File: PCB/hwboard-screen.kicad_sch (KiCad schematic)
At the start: 1 part, among them J1 Conn_01x40

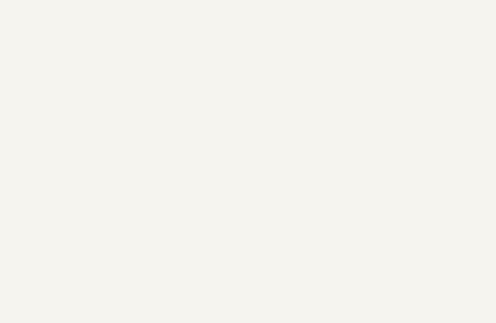
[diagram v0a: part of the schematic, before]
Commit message: add resistive touch IC
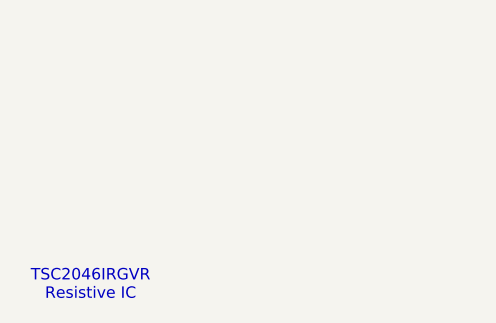
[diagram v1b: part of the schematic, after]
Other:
- note added: "TSC2046IRGVR Resistive IC"
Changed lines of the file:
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@@
 	(generator_version "9.0")
 	(paper "A4")
+	(text "TSC2046IRGVR\nResistive IC"
+		(exclude_from_sim no)
+		(at 111.252 159.258 0)
+		(effects
+			(font
+				(size 1.27 1.27)
+			)
+		)
+	)
 	(symbol
 		(lib_id "Connector_Generic:Conn_01x40")

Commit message: add maybe layout and pcb for screen
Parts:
- removed J1: Conn_01x40, symbol Connector_Generic:Conn_01x40
- added DISP1: QD3508, G__project_3.5inch_3.5inch_common_spi_ctp_PCB_3.5inch_Common_SPI_CTP.PcbLib:3.5-QD3503, symbol hwboard-bike-computer:QD3508
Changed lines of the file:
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@@
 	)
 	(symbol
-		(lib_id "Connector_Generic:Conn_01x40")
-		(at 201.93 88.9 0)
+		(lib_id "hwboard-bike-computer:QD3508")
+		(at 173.99 30.48 0)
 		(unit 1)
 		(exclude_from_sim no)
@@
 		(dnp no)
 		(fields_autoplaced yes)
-		(property "Reference" "J1"
-			(at 204.47 88.8999 0)
+		(property "Reference" "DISP1"
+			(at 195.58 90.8049 0)
 			(effects
 				(font
-					(size 1.27 1.27)
+					(size 1.8288 1.8288)
 				)
 				(justify left)
 			)
 		)
-		(property "Value" "Conn_01x40"
-			(at 204.47 91.4399 0)
+		(property "Value" "QD3508"
+			(at 195.58 94.6149 0)
 			(effects
 				(font
-					(size 1.27 1.27)
+					(size 1.8288 1.8288)
 				)
 				(justify left)
 			)
 		)
-		(property "Footprint" ""
-			(at 201.93 88.9 0)
+		(property "Footprint" "G__project_3.5inch_3.5inch_common_spi_ctp_PCB_3.5inch_Common_SPI_CTP.PcbLib:3.5-QD3503"
+			(at 173.99 30.48 0)
 			(effects
 				(font
@@
 			)
 		)
-		(property "Datasheet" "~"
-			(at 201.93 88.9 0)
+		(property "Datasheet" ""
+			(at 173.99 30.48 0)
 			(effects
 				(font
@@
 			)
 		)
-		(property "Description" "Generic connector, single row, 01x40, script generated (kicad-library-utils/schlib/autogen/connector/)"
-			(at 201.93 88.9 0)
+		(property "Description" ""
+			(at 173.99 30.48 0)
 			(effects
 				(font
@@
 			)
 		)
-		(pin "31"
-		)
 		(pin "38"
-		)
-		(pin "8"
-		)
-		(pin "20"
-		)
-		(pin "18"
-		)
-		(pin "11"
-		)
-		(pin "34"
-		)
-		(pin "23"
-		)
-		(pin "39"
-		)
-		(pin "35"
-		)
-		(pin "27"
-		)
-		(pin "36"
-		)
-		(pin "28"
 		)
 		(pin "29"
 		)
-		(pin "24"
-		)
-		(pin "12"
-		)
-		(pin "25"
-		)
-		(pin "26"
-		)
-		(pin "37"
-		)
-		(pin "9"
-		)
-		(pin "13"
-		)
-		(pin "3"
-		)
-		(pin "1"
+		(pin "22"
 		)
 		(pin "4"
-		)
-		(pin "2"
-		)
-		(pin "5"
-		)
-		(pin "10"
-		)
-		(pin "17"
-		)
-		(pin "14"
-		)
-		(pin "40"
-		)
-		(pin "30"
-		)
-		(pin "33"
-		)
-		(pin "19"
-		)
-		(pin "22"
 		)
 		(pin "7"
@@
 		(pin "6"
 		)
-		(pin "16"
+		(pin "5"
+		)
+		(pin "2"
+		)
+		(pin "1"
+		)
+		(pin "19"
+		)
+		(pin "17"
+		)
+		(pin "39"
 		)
 		(pin "21"
 		)
+		(pin "35"
+		)
+		(pin "18"
+		)
+		(pin "8"
+		)
+		(pin "15"
+		)
+		(pin "16"
+		)
+		(pin "43"
+		)
+		(pin "44"
+		)
+		(pin "34"
+		)
+		(pin "10"
+		)
+		(pin "33"
+		)
+		(pin "36"
+		)
+		(pin "40"
+		)
+		(pin "28"
+		)
+		(pin "23"
+		)
+		(pin "42"
+		)
+		(pin "11"
+		)
+		(pin "45"
+		)
+		(pin "30"
+		)
+		(pin "27"
+		)
+		(pin "48"
+		)
+		(pin "37"
+		)
+		(pin "25"
+		)
+		(pin "24"
+		)
+		(pin "47"
+		)
+		(pin "26"
+		)
+		(pin "41"
+		)
+		(pin "9"
+		)
+		(pin "31"
+		)
 		(pin "32"
 		)
-		(pin "15"
+		(pin "12"
+		)
+		(pin "20"
+		)
+		(pin "14"
+		)
+		(pin "46"
+		)
+		(pin "3"
+		)
+		(pin "13"
 		)
 		(instances
 			(project ""
 				(path "/8c0f76b9-ee42-4bcf-bb95-09772e367402/4b830c8b-a993-4513-b498-b6b511f6381b"
-					(reference "J1")
+					(reference "DISP1")
 					(unit 1)
 				)
